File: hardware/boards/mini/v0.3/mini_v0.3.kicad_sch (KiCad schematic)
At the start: 95 parts, among them IC1 NAU88C22YG, IC3 IS42S16160J-6BLI, J2 Top (A), J3 Bottom (B), J4 DF40C-90DP-0.4V, U1 W25Q128JVP, U2 LTV-217-G, U4 STM32H750XBHx, Y1 Crystal_GND24, Y3 32.768kHz

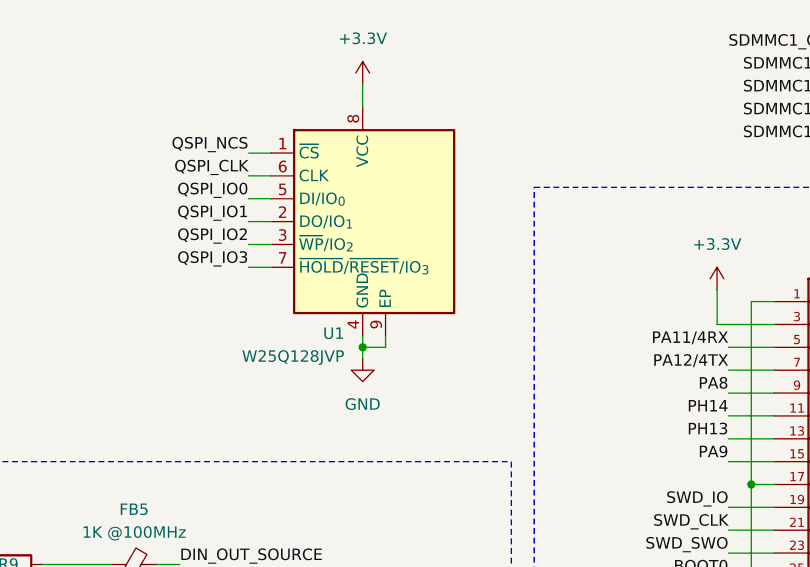
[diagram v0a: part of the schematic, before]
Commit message: mini: change flash to SOIC8 to fix routing
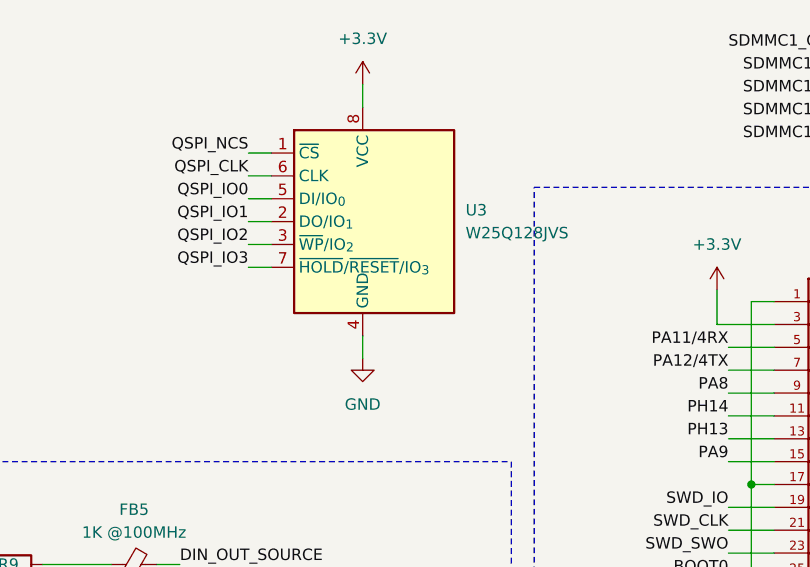
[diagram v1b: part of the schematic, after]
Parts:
- removed U1: W25Q128JVP, Package_SON:WSON-8-1EP_6x5mm_P1.27mm_EP3.4x4.3mm, symbol Memory_Flash:W25Q128JVP
- added U3: W25Q128JVS, Package_SO:SOIC-8_5.3x5.3mm_P1.27mm, symbol Memory_Flash:W25Q128JVS
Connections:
- net +3.3V: now also U3.8 (VCC)
- net GND: now also U3.4 (GND)
- net QSPI_CLK: now also U3.6 (CLK)
- net QSPI_IO0: now also U3.5 (DI/IO_{0})
- net QSPI_IO1: now also U3.2 (DO/IO_{1})
- net QSPI_IO2: now also U3.3 (~{WP}/IO_{2})
- net QSPI_IO3: now also U3.7 (~{HOLD}/~{RESET}/IO_{3})
- net QSPI_NCS: now also U3.1 (~{CS})
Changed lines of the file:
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@@
 	)
 	(junction
-		(at 309.88 67.31)
-		(diameter 0)
-		(color 0 0 0 0)
-	)
-	(junction
 		(at 134.62 22.86)
 		(diameter 0)
@@
 	(wire
 		(pts
-			(xy 312.42 67.31) (xy 312.42 66.04)
-		)
-		(stroke
-			(width 0)
-			(type default)
-		)
-	)
-	(wire
-		(pts
 			(xy 157.48 86.36) (xy 157.48 93.98)
 		)
@@
 	(wire
 		(pts
-			(xy 309.88 67.31) (xy 309.88 68.58)
+			(xy 309.88 66.04) (xy 309.88 68.58)
 		)
 		(stroke
@@
 	(wire
 		(pts
-			(xy 309.88 67.31) (xy 312.42 67.31)
-		)
-		(stroke
-			(width 0)
-			(type default)
-		)
-	)
-	(wire
-		(pts
 			(xy 177.8 160.02) (xy 181.61 160.02)
 		)
@@
 	(wire
 		(pts
-			(xy 309.88 66.04) (xy 309.88 67.31)
-		)
-		(stroke
-			(width 0)
-			(type default)
-		)
-	)
-	(wire
-		(pts
 			(xy 486.41 133.35) (xy 488.95 133.35)
 		)
@@
 	)
 	(symbol
+		(lib_id "Memory_Flash:W25Q128JVS")
+		(at 309.88 53.34 0)
+		(unit 1)
+		(exclude_from_sim no)
+		(in_bom yes)
+		(on_board yes)
+		(dnp no)
+		(fields_autoplaced yes)
+		(property "Reference" "U3"
+			(at 321.31 52.0699 0)
+			(effects
+				(font
+					(size 1.27 1.27)
+				)
+				(justify left)
+			)
+		)
+		(property "Value" "W25Q128JVS"
+			(at 321.31 54.6099 0)
+			(effects
+				(font
+					(size 1.27 1.27)
+				)
+				(justify left)
+			)
+		)
+		(property "Footprint" "Package_SO:SOIC-8_5.3x5.3mm_P1.27mm"
+			(at 309.88 30.48 0)
+			(effects
+				(font
+					(size 1.27 1.27)
+				)
+				(hide yes)
+			)
+		)
+		(property "Datasheet" "https://www.winbond.com/resource-files/w25q128jv_dtr%20revc%2003272018%20plus.pdf"
+			(at 309.88 27.94 0)
+			(effects
+				(font
+					(size 1.27 1.27)
+				)
+				(hide yes)
+			)
+		)
+		(property "Description" "128Mbit / 16MiB Serial Flash Memory, Standard/Dual/Quad SPI, 2.7-3.6V, SOIC-8"
+			(at 309.88 25.4 0)
+			(effects
+				(font
+					(size 1.27 1.27)
+				)
+				(hide yes)
+			)
+		)
+		(pin "8"
+		)
+		(pin "4"
+		)
+		(pin "7"
+		)
+		(pin "2"
+		)
+		(pin "3"
+		)
+		(pin "5"
+		)
+		(pin "6"
+		)
+		(pin "1"
+		)
+		(instances
+			(project ""
+				(path "/f8dd7a9e-fcd3-404d-b8a5-ab89fe05940b"
+					(reference "U3")
+					(unit 1)
+				)
+			)
+		)
+	)
+	(symbol
 		(lib_id "Device:C_Small")
 		(at 233.68 55.88 0)
@@
 					(unit 1)
 				)
-			)
-		)
-	)
-	(symbol
-		(lib_id "Memory_Flash:W25Q128JVP")
-		(at 309.88 53.34 0)
-		(unit 1)
-		(exclude_from_sim no)
-		(in_bom yes)
-		(on_board yes)
-		(dnp no)
-		(property "Reference" "U1"
-			(at 307.848 65.786 0)
-			(effects
-				(font
-					(size 1.27 1.27)
-				)
-				(justify right)
-			)
-		)
-		(property "Value" "W25Q128JVP"
-			(at 307.848 68.326 0)
-			(effects
-				(font
-					(size 1.27 1.27)
-				)
-				(justify right)
-			)
-		)
-		(property "Footprint" "Package_SON:WSON-8-1EP_6x5mm_P1.27mm_EP3.4x4.3mm"
-			(at 309.88 30.48 0)
-			(effects
-				(font
-					(size 1.27 1.27)
-				)
-				(hide yes)
-			)
-		)
-		(property "Datasheet" "https://www.winbond.com/resource-files/w25q128jv_dtr%20revc%2003272018%20plus.pdf"
-			(at 309.88 27.94 0)
-			(effects
-				(font
-					(size 1.27 1.27)
-				)
-				(hide yes)
-			)
-		)
-		(property "Description" "128Mbit / 16MiB Serial Flash Memory, Standard/Dual/Quad SPI, 2.7-3.6V, WSON-8"
-			(at 309.88 25.4 0)
-			(effects
-				(font
-					(size 1.27 1.27)
-				)
-				(hide yes)
-			)
-		)
-		(property "LCSC" "C190862"
-			(at 309.88 53.34 0)
-			(effects
-				(font
-					(size 1.27 1.27)
-				)
-				(hide yes)
-			)
-		)
-		(pin "1"
-		)
-		(pin "6"
-		)
-		(pin "5"
-		)
-		(pin "2"
-		)
-		(pin "3"
-		)
-		(pin "9"
-		)
-		(pin "8"
-		)
-		(pin "7"
-		)
-		(pin "4"
-		)
-		(instances
-			(project ""
-				(path "/f8dd7a9e-fcd3-404d-b8a5-ab89fe05940b"
-					(reference "U1")
-					(unit 1)
-				)
